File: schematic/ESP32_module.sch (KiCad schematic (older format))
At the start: 10 parts

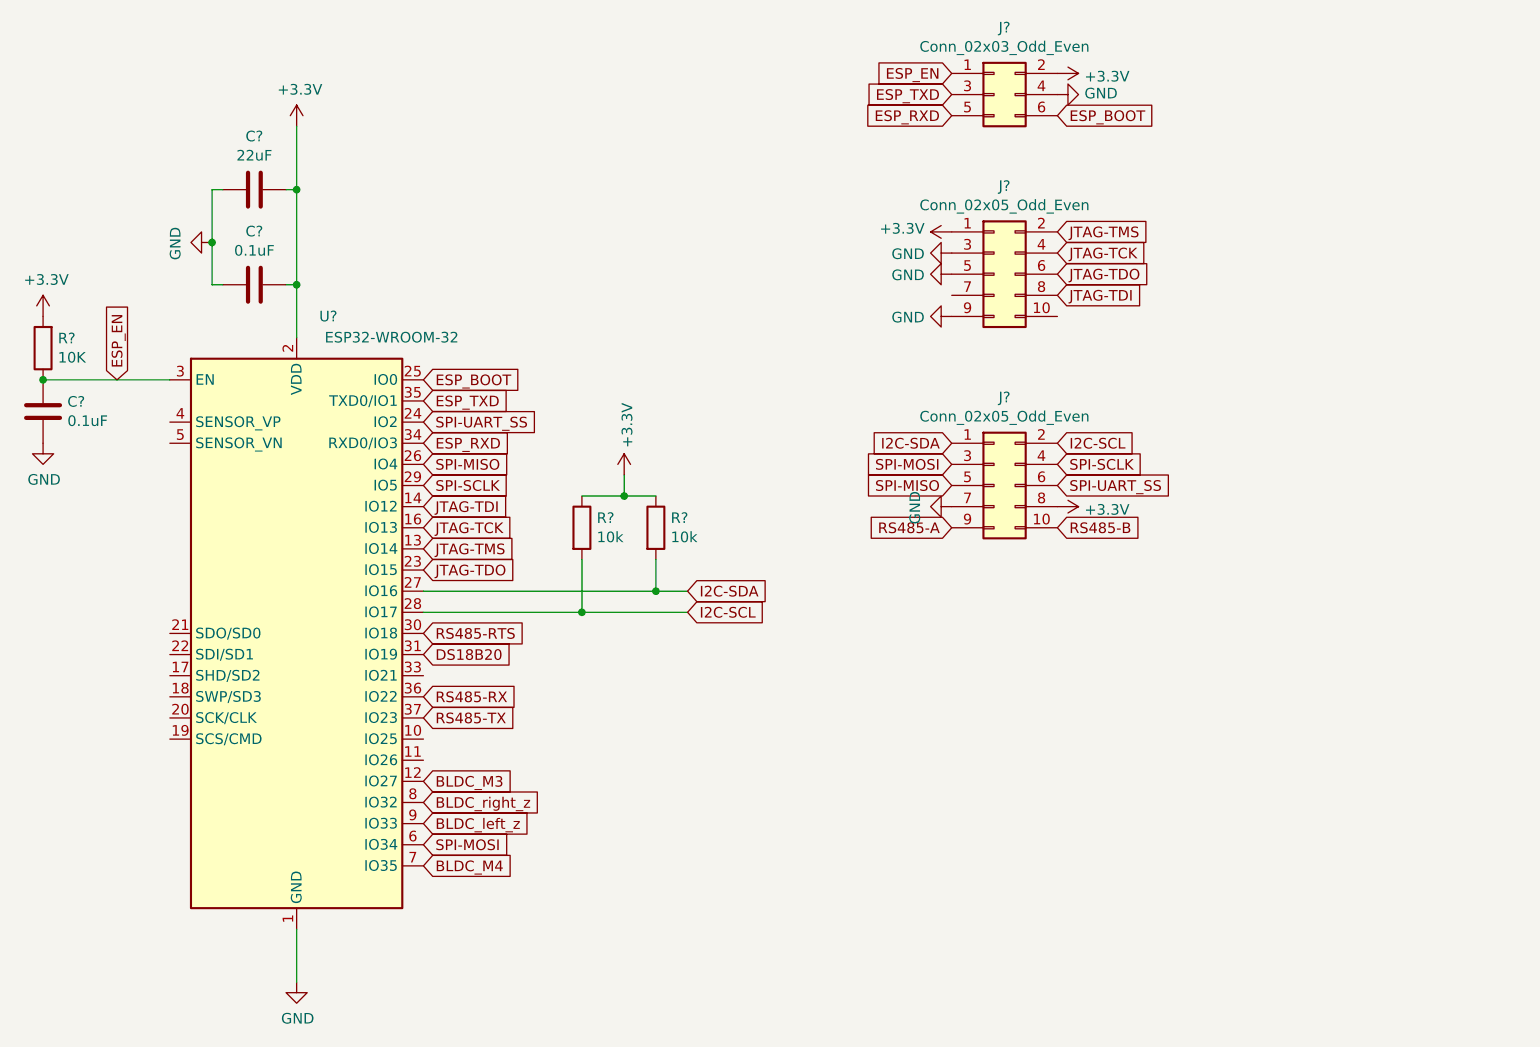
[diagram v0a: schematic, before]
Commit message: prototype footprint and placement test
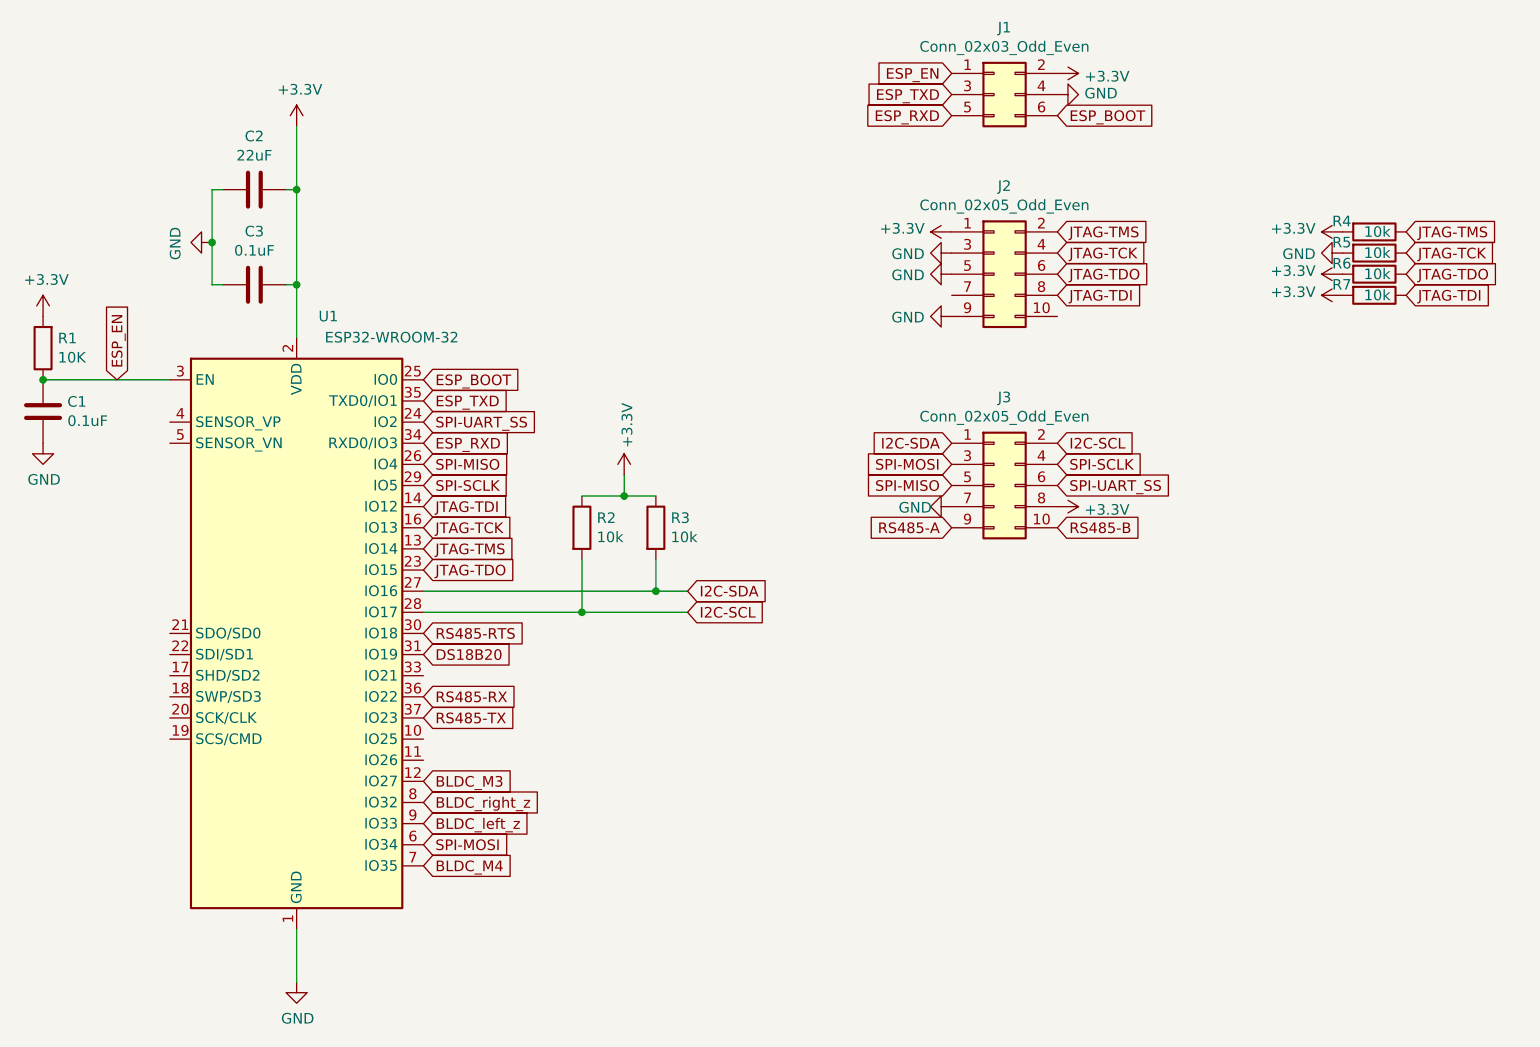
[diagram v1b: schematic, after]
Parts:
- added R4, R5, R6, R7: 10k, Resistor_SMD:R_0805_2012Metric_Pad1.15x1.40mm_HandSolder, symbol Device:R
- C1, C2, C3: renamed from C?; footprint (none) -> Capacitor_SMD:C_0805_2012Metric_Pad1.15x1.40mm_HandSolder
- J1: renamed from J?; footprint (none) -> Connector_IDC:IDC-Header_2x03_P2.54mm_Vertical
- J2, J3: renamed from J?; footprint (none) -> Connector_IDC:IDC-Header_2x05_P2.54mm_Vertical
- R1, R2, R3: renamed from R?; footprint (none) -> Resistor_SMD:R_0805_2012Metric_Pad1.15x1.40mm_HandSolder
- gave numbers to parts that had none: 1
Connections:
- net +3V3: now also R4.2, R6.2, R7.2
- net GND: now also R5.2
- net JTAG-TCK: now also R5.1
- net JTAG-TDI: now also R7.1
- net JTAG-TDO: now also R6.1
- net JTAG-TMS: now also R4.1

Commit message: added LSM6DSOX and LIS2MDL for IMU
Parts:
- J1: footprint Connector_IDC:IDC-Header_2x03_P2.54mm_Vertical -> Connector_PinHeader_1.27mm:PinHeader_2x03_P1.27mm_Vertical_SMD
- J2: footprint Connector_IDC:IDC-Header_2x05_P2.54mm_Vertical -> Connector_PinHeader_1.27mm:PinHeader_2x05_P1.27mm_Vertical_SMD
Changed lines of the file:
@@
 F 0 "J1" H 5900 2067 50  0000 C CNN
 F 1 "Conn_02x03_Odd_Even" H 5900 1976 50  0000 C CNN
-F 2 "Connector_IDC:IDC-Header_2x03_P2.54mm_Vertical" H 5850 1750 50  0001 C CNN
+F 2 "Connector_PinHeader_1.27mm:PinHeader_2x03_P1.27mm_Vertical_SMD" H 5850 1750 50  0001 C CNN
 F 3 "~" H 5850 1750 50  0001 C CNN
 	1    5850 1750
@@
 F 0 "J2" H 5900 3017 50  0000 C CNN
 F 1 "Conn_02x05_Odd_Even" H 5900 2926 50  0000 C CNN
-F 2 "Connector_IDC:IDC-Header_2x05_P2.54mm_Vertical" H 5850 2600 50  0001 C CNN
+F 2 "Connector_PinHeader_1.27mm:PinHeader_2x05_P1.27mm_Vertical_SMD" H 5850 2600 50  0001 C CNN
 F 3 "~" H 5850 2600 50  0001 C CNN
 	1    5850 2600
